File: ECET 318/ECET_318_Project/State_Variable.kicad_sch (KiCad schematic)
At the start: 25 parts, among them U10 TL082, U4 TL084

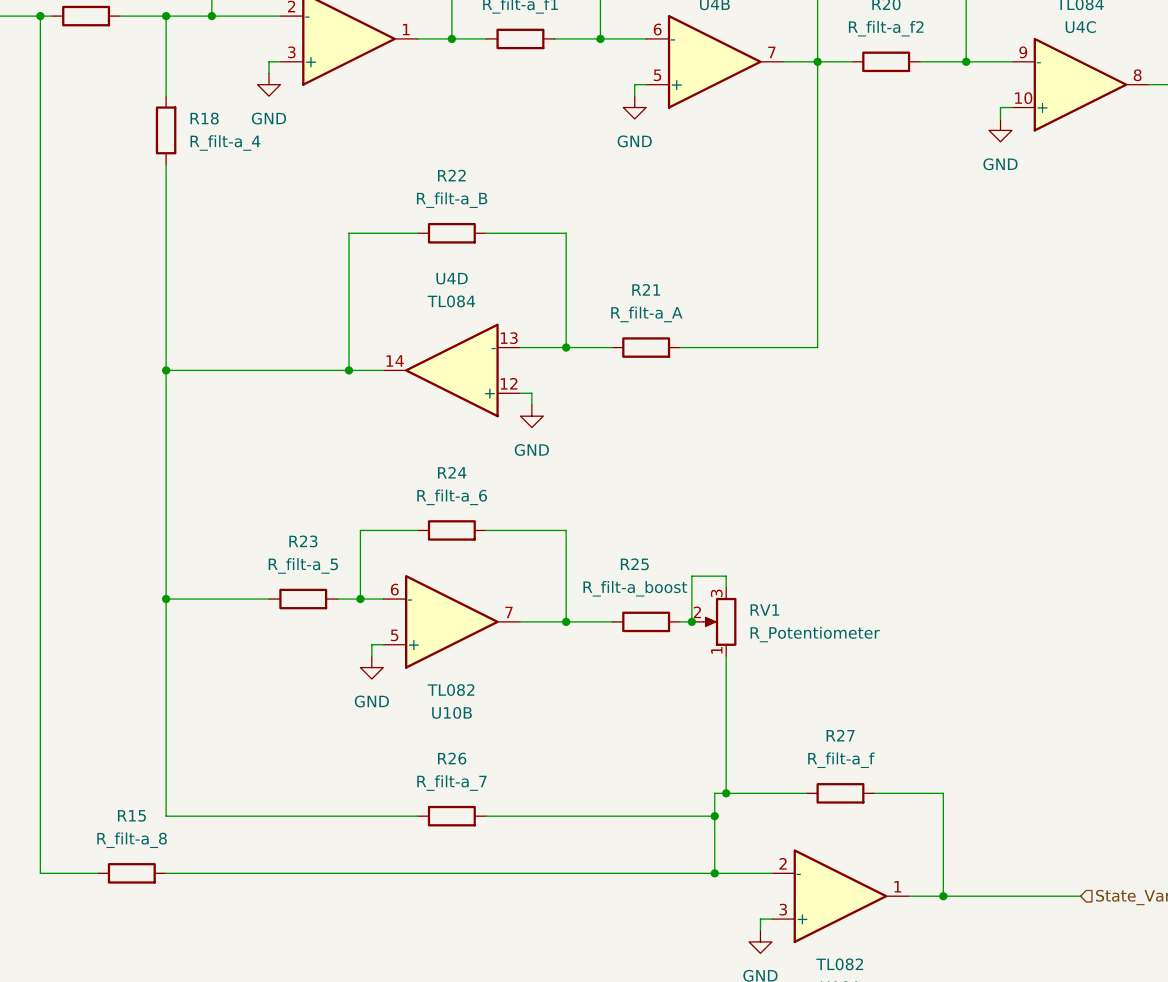
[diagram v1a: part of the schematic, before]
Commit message: Added Breadboard Space and Test Points
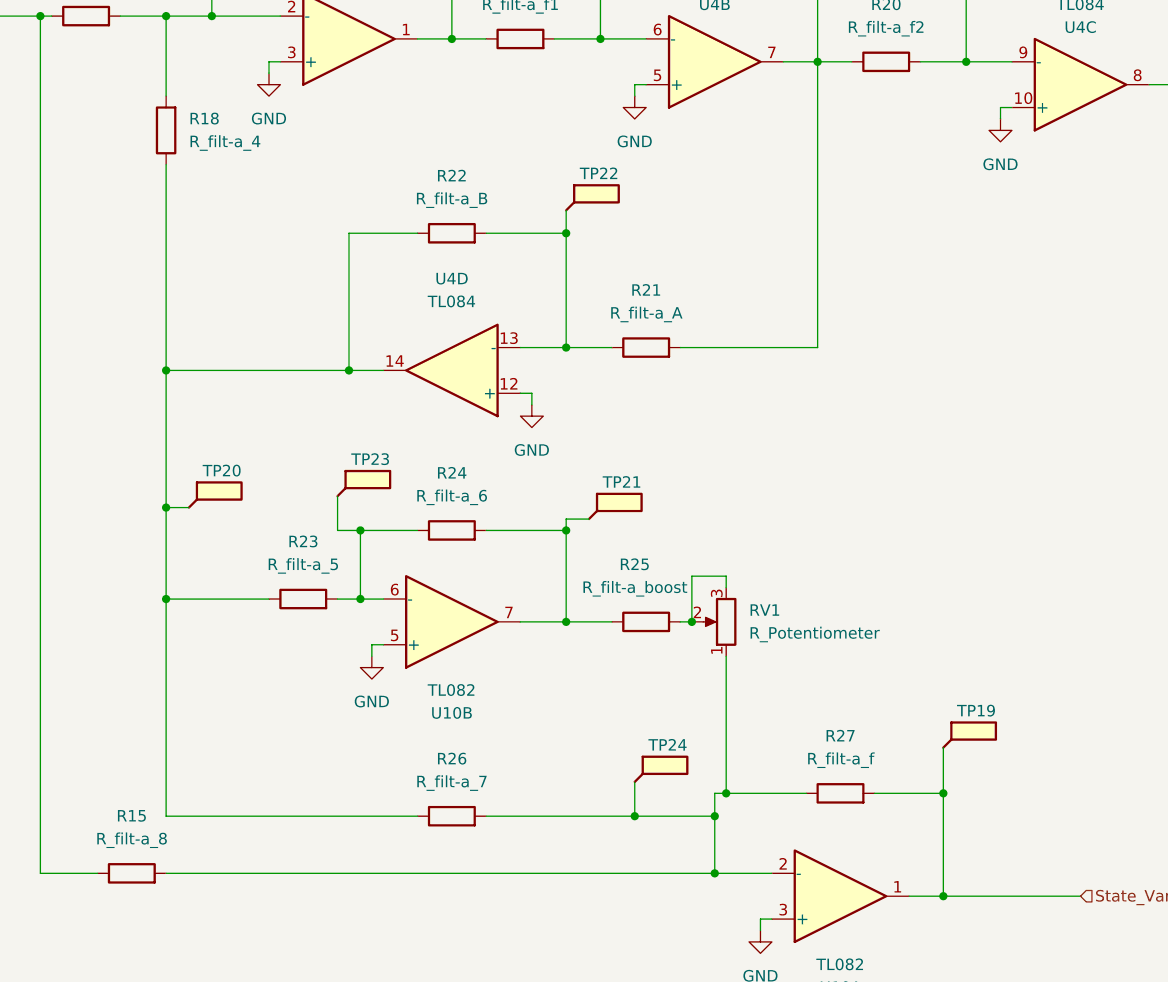
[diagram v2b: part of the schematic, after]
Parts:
- added TP19, TP20, TP21, TP22, TP23, TP24: TestPoint_Flag, TestPoint:TestPoint_Pad_D1.5mm, symbol Connector:TestPoint_Flag
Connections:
- net State_Variable_Out: now also TP19.1
- net at R23.2, R24.1, U10.6 (-): now also TP23.1
- net at R24.2, R25.1, U10.7: now also TP21.1
- net at R18.1, R22.1, R23.1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: now also TP20.1
- net at R15.2, R26.2, R27.1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: now also TP24.1
- net at R21.1, R22.2, U4.13 (-): now also TP22.1
